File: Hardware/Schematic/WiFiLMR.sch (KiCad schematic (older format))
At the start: 8 parts, among them J1 Conn_01x03_Male, J2 Conn_01x02_Male, J3 Conn_01x04_Male, U1 ESP32-WROOM-32U

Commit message: Particle Photon Schematic Update
Added Particle Photon symbol, footprint & 3D model along with datasheet. Updated schematic with sockets to plugin a Photon board and a JTAG connector based off of the design in the Photon datasheet.
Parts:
- removed C1, C2, C3: 0.1uF, Capacitor_SMD:C_0603_1608Metric_Pad1.05x0.95mm_HandSolder, symbol Device:C
- removed J1: Conn_01x03_Male, Connector_PinHeader_2.54mm:PinHeader_1x03_P2.54mm_Vertical, symbol Connector:Conn_01x03_Male
- removed J2: Conn_01x02_Male, Connector_PinHeader_2.54mm:PinHeader_1x02_P2.54mm_Vertical, symbol Connector:Conn_01x02_Male
- removed J3: Conn_01x04_Male, Connector_PinHeader_2.54mm:PinHeader_1x04_P2.54mm_Vertical, symbol Connector:Conn_01x04_Male
- removed R1: 10K, Resistor_SMD:R_0603_1608Metric_Pad1.05x0.95mm_HandSolder, symbol Device:R_US
- removed U1: ESP32-WROOM-32U, RF_Module:ESP32-WROOM-32U, symbol RF_Module:ESP32-WROOM-32U
- added J1, J2: Conn_01x12, Connector_PinSocket_2.54mm:PinSocket_1x12_P2.54mm_Vertical, symbol Connector_Generic:Conn_01x12
- added J3: JTAG, Connector_PinHeader_2.54mm:PinHeader_2x10_P2.54mm_Vertical, symbol Connector_Generic:Conn_02x10_Odd_Even
- added MODULE1: WRL-13764, SPARKFUN_WRL-13764, symbol WRL-13764:WRL-13764
- added R1, R2, R3, R4: R_Small_US, Resistor_SMD:R_2512_6332Metric_Pad1.52x3.35mm_HandSolder, symbol Device:R_Small_US
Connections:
- net labels added: +3V3, JTAG_RESET, TCK, TDI, TDO, TMS, TRST
- net labels removed: +3.3V
- wire segments 33 -> 50

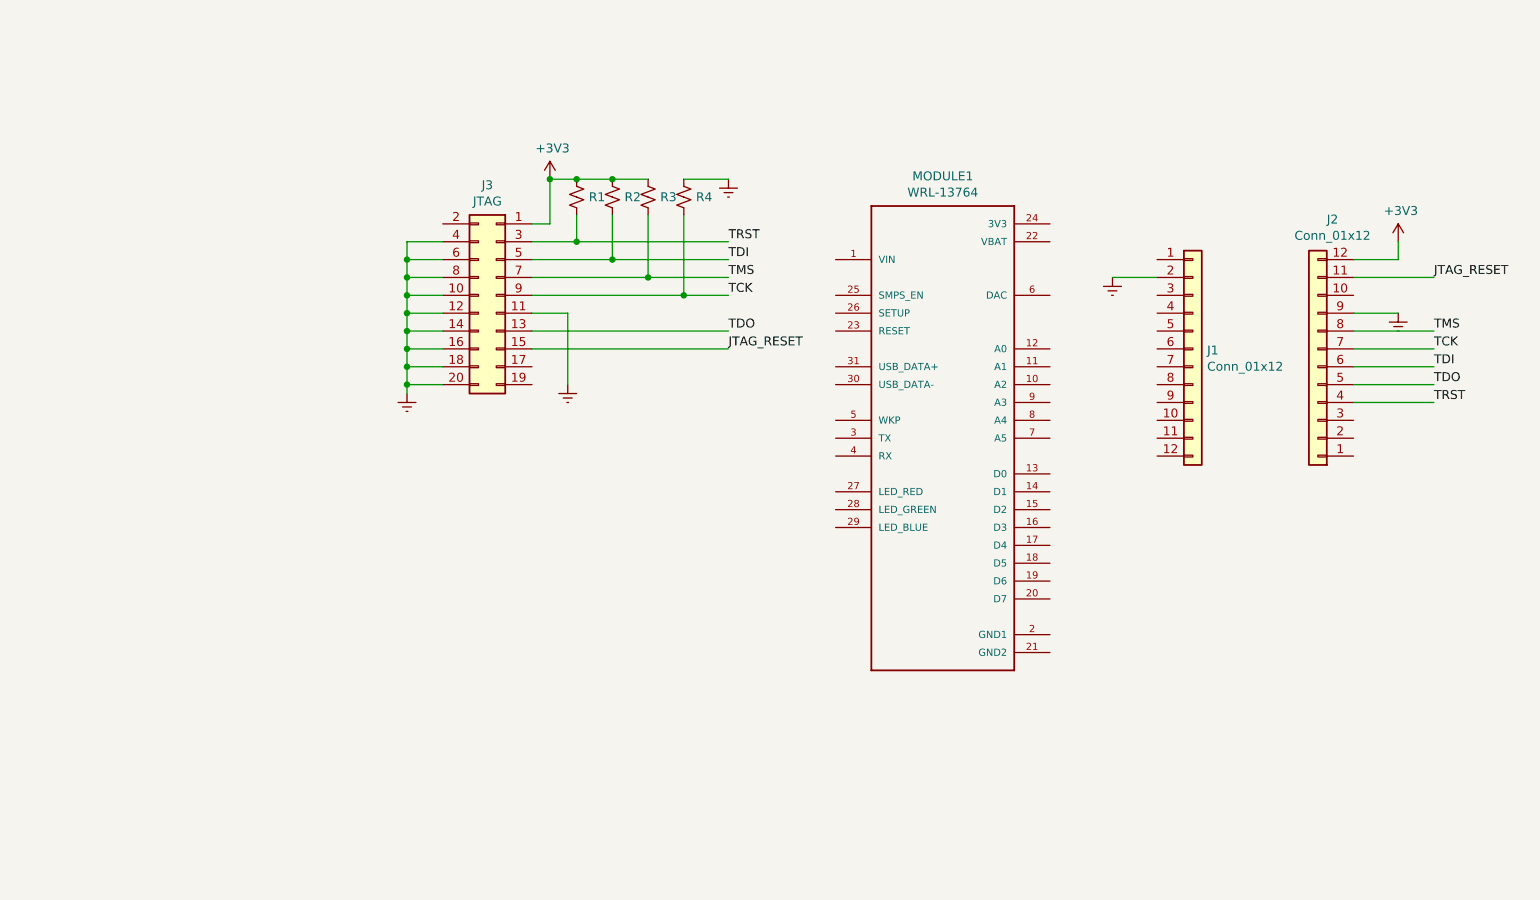
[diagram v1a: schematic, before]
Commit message: Update schematic with JTAG and debug headers
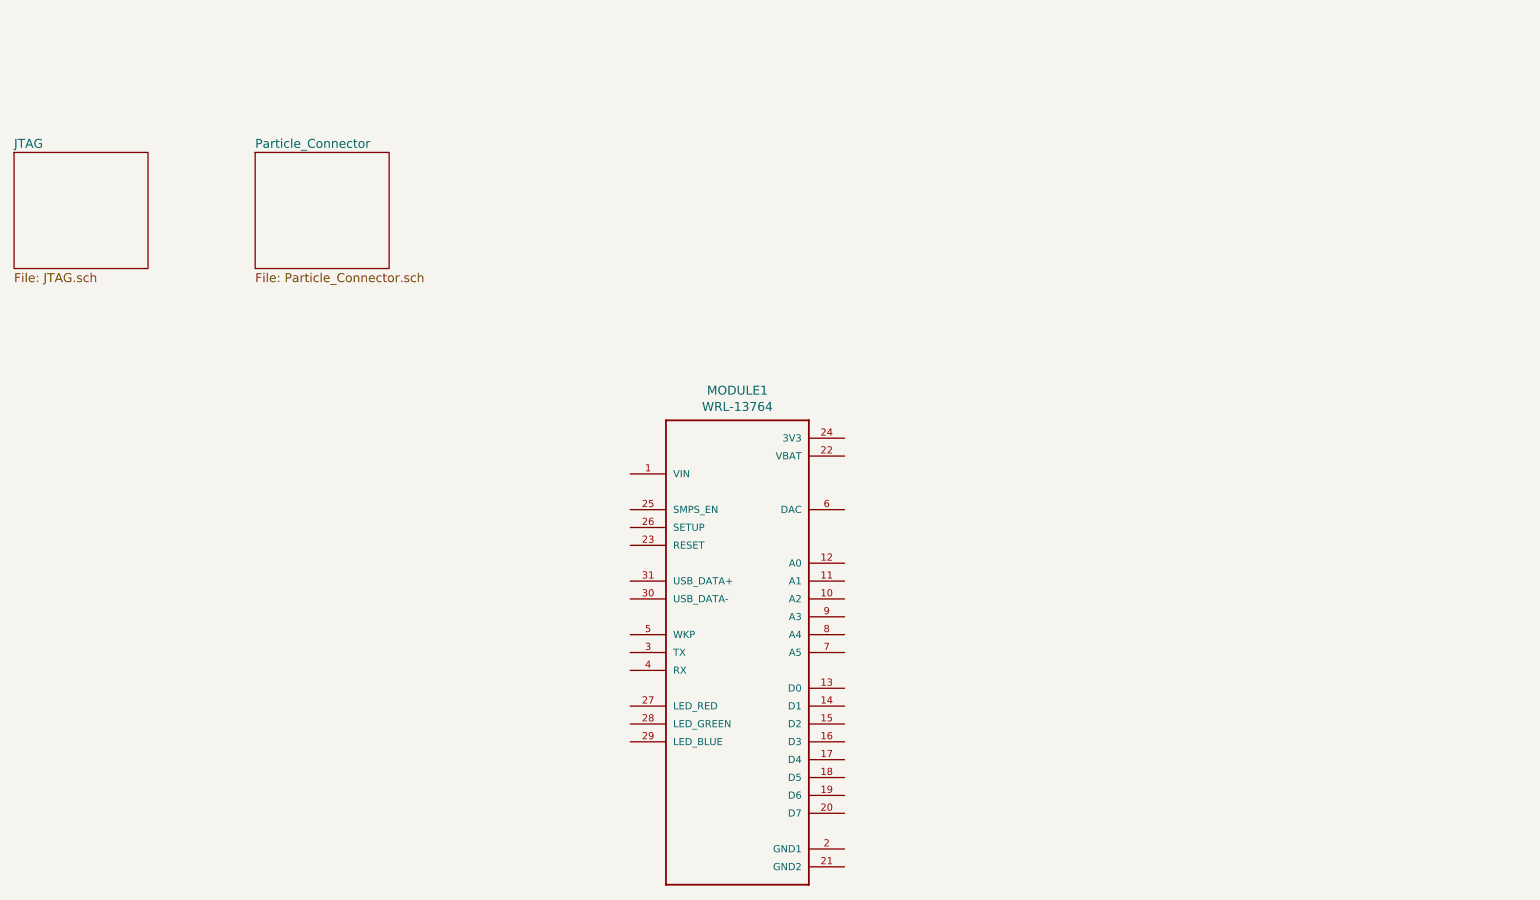
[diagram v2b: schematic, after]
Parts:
- removed J1, J2: Conn_01x12, Connector_PinSocket_2.54mm:PinSocket_1x12_P2.54mm_Vertical, symbol Connector_Generic:Conn_01x12
- removed J3: JTAG, Connector_PinHeader_2.54mm:PinHeader_2x10_P2.54mm_Vertical, symbol Connector_Generic:Conn_02x10_Odd_Even
- removed R1, R2, R3, R4: R_Small_US, Resistor_SMD:R_2512_6332Metric_Pad1.52x3.35mm_HandSolder, symbol Device:R_Small_US
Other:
- moved on the sheet: MODULE1

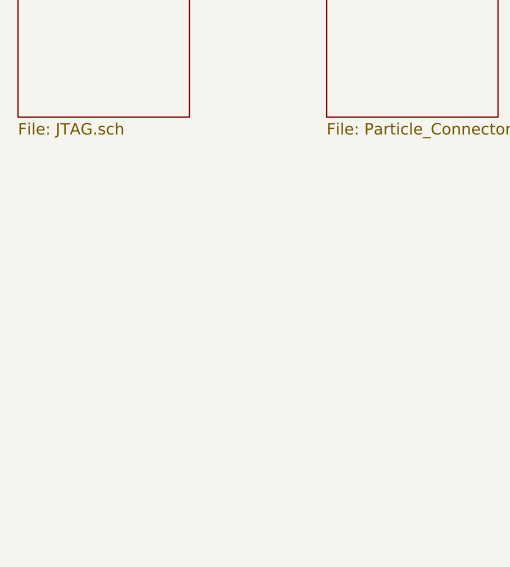
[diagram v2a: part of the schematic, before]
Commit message: Added TCA8418 keyscan module to the schematic
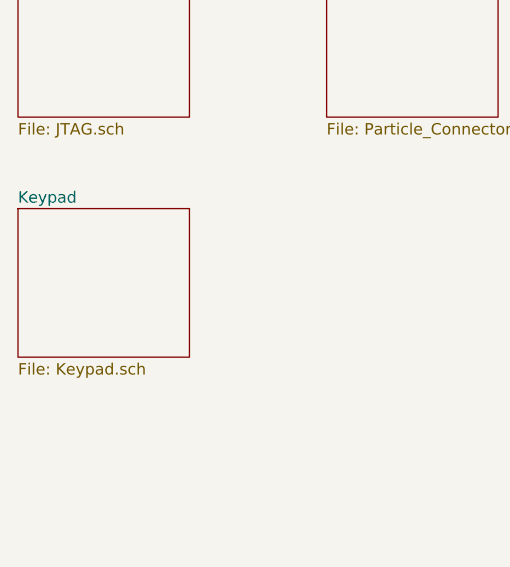
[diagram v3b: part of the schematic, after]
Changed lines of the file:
@@
 $Descr A4 11693 8268
 encoding utf-8
-Sheet 1 3
+Sheet 1 4
 Title ""
 Date ""
@@
 F1 "Particle_Connector.sch" 50
 $EndSheet
+$Sheet
+S 2050 3300 750  650
+U 5D1772AD
+F0 "Keypad" 50
+F1 "Keypad.sch" 50
+$EndSheet
 $EndSCHEMATC

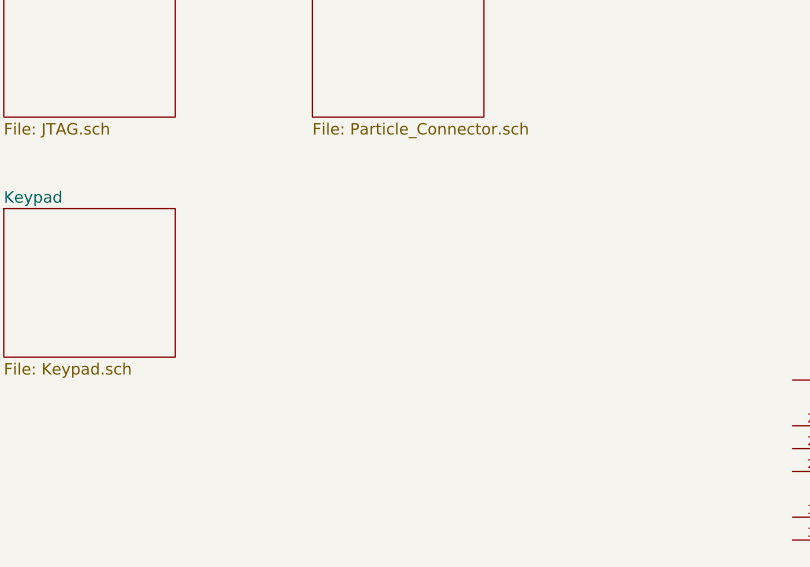
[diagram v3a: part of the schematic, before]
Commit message: Added E-INK display connector and datasheet
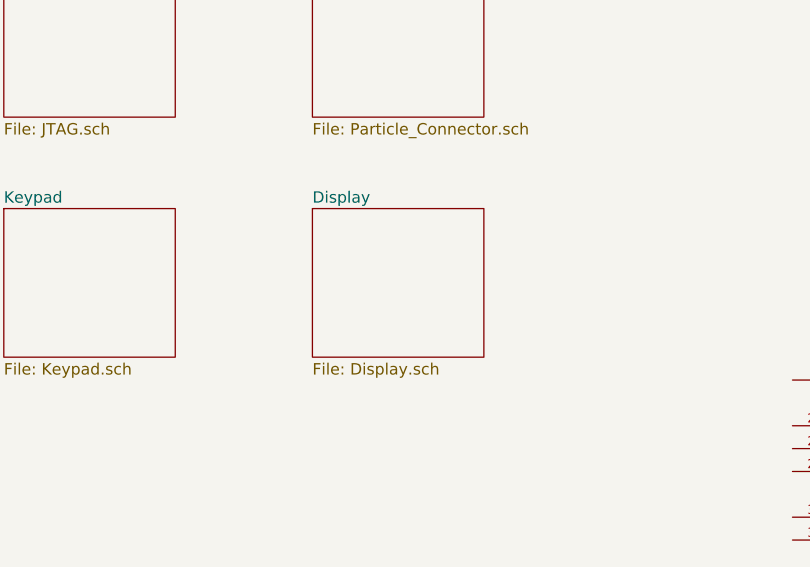
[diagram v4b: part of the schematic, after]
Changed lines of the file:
@@
 $Descr A4 11693 8268
 encoding utf-8
-Sheet 1 4
+Sheet 1 5
 Title ""
 Date ""
@@
 F1 "Keypad.sch" 50
 $EndSheet
+$Sheet
+S 3400 3300 750  650
+U 5D193223
+F0 "Display" 50
+F1 "Display.sch" 50
+$EndSheet
 $EndSCHEMATC

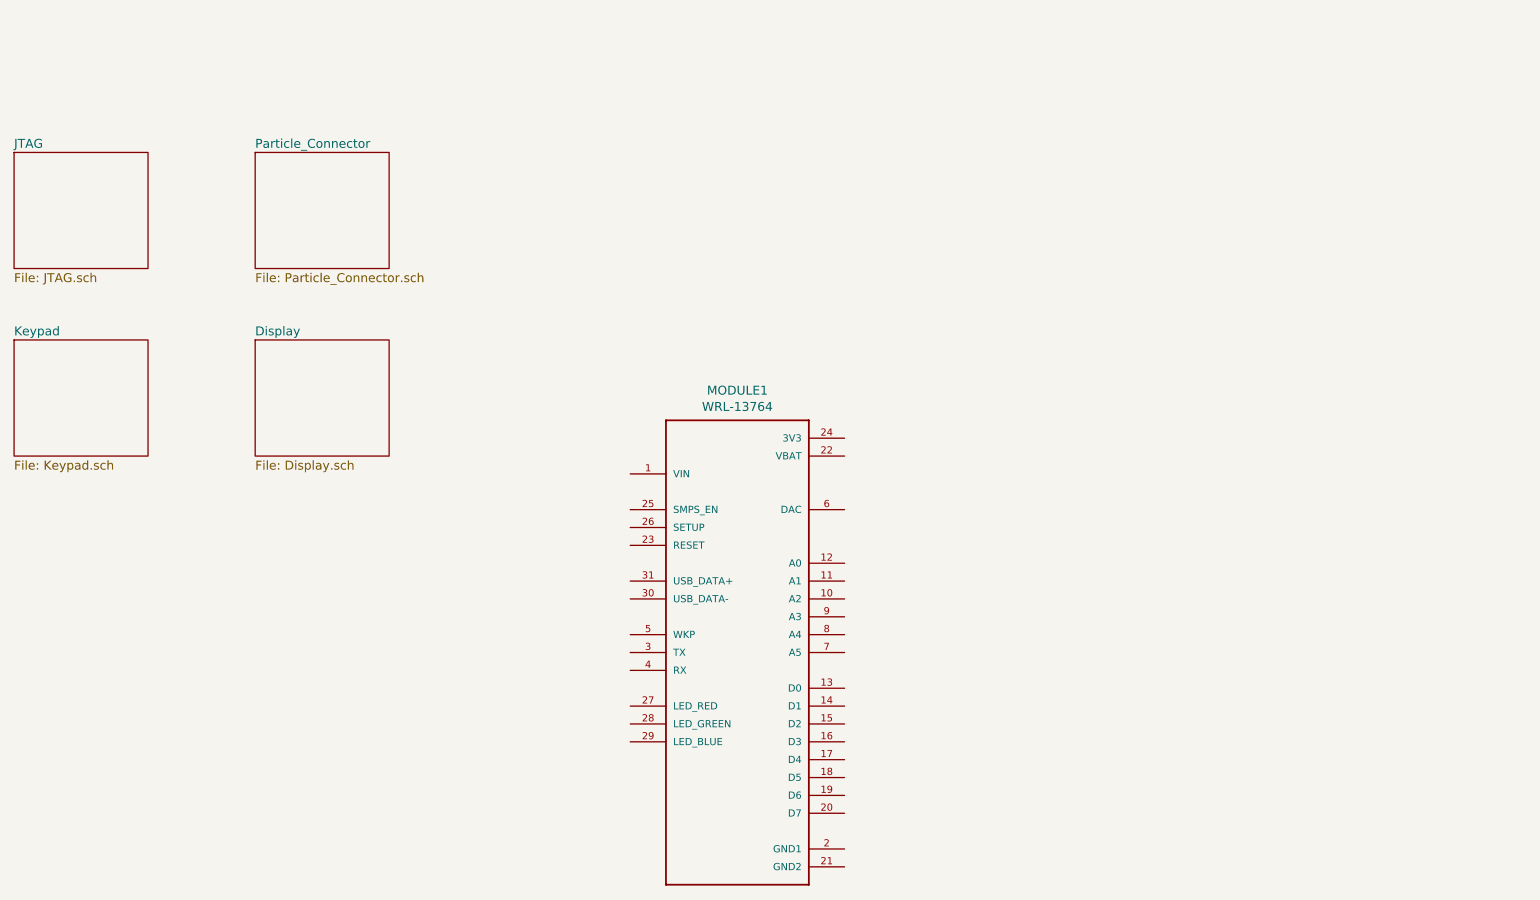
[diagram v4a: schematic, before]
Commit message: Lots of schematic updates
Lots of stuff...

* Added a new 8-pin TVS diode array
* Finalized the display connector
* Corrected the net labels to global labels so they span across sheets
* Added a 5V linear voltage regulator and LEDs to debug power
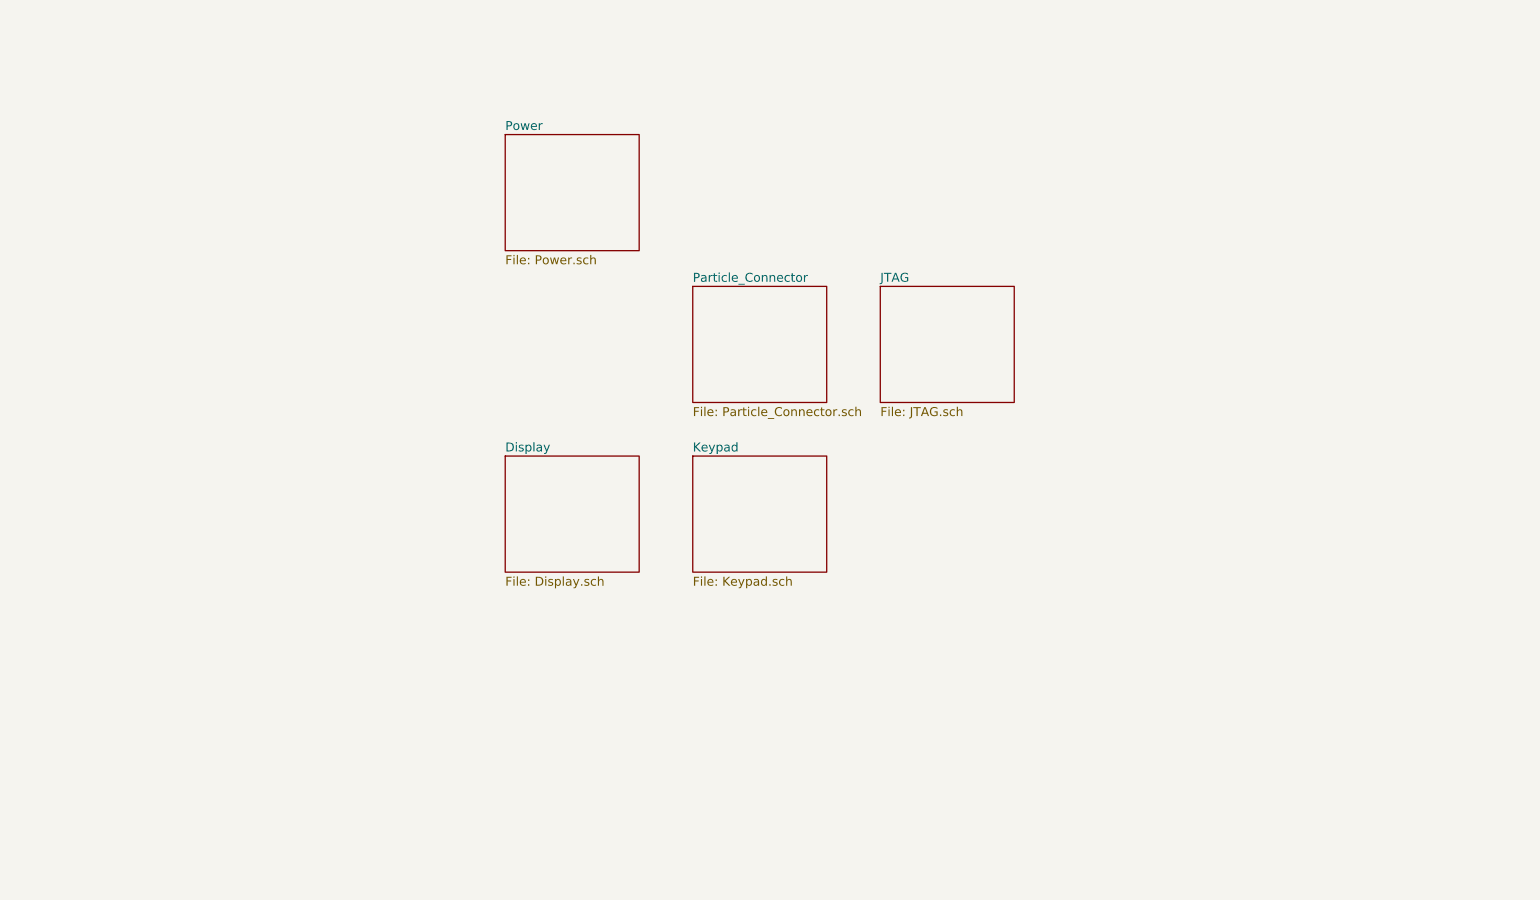
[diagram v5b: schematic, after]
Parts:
- removed MODULE1: WRL-13764, SPARKFUN_WRL-13764, symbol WRL-13764:WRL-13764
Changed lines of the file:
@@
 $Descr A4 11693 8268
 encoding utf-8
-Sheet 1 5
+Sheet 1 6
 Title ""
 Date ""
@@
 Comment4 ""
 $EndDescr
-$Comp
-L WRL-13764:WRL-13764 MODULE1
-U 1 1 5CF72957
-P 6100 5050
-F 0 "MODULE1" H 6100 6517 50  0000 C CNN
-F 1 "WRL-13764" H 6100 6426 50  0000 C CNN
-F 2 "SPARKFUN_WRL-13764" H 6100 5050 50  0001 L BNN
-F 3 "" H 6100 5050 50  0001 L BNN
-F 4 "WRL-13764" H 6100 5050 50  0001 L BNN "Field4"
-F 5 "Unavailable" H 6100 5050 50  0001 L BNN "Field5"
-F 6 "None" H 6100 5050 50  0001 L BNN "Field6"
-F 7 "SparkFun Electronics" H 6100 5050 50  0001 L BNN "Field7"
-F 8 "Particle Photon _No Headers_" H 6100 5050 50  0001 L BNN "Field8"
-	1    6100 5050
-	1    0    0    -1
-$EndComp
 $Sheet
-S 2050 2250 750  650
+S 6900 3000 750  650
 U 5CFB0E28
 F0 "JTAG" 50
@@
 $EndSheet
 $Sheet
-S 3400 2250 750  650
+S 5850 3000 750  650
 U 5D01AE82
 F0 "Particle_Connector" 50
@@
 $EndSheet
 $Sheet
-S 2050 3300 750  650
+S 5850 3950 750  650
 U 5D1772AD
 F0 "Keypad" 50
@@
 $EndSheet
 $Sheet
-S 3400 3300 750  650
+S 4800 3950 750  650
 U 5D193223
 F0 "Display" 50
 F1 "Display.sch" 50
 $EndSheet
+$Sheet
+S 4800 2150 750  650
+U 5D21B5D5
+F0 "Power" 50
+F1 "Power.sch" 50
+$EndSheet
 $EndSCHEMATC
